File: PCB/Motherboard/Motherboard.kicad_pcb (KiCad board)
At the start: 2 copper layers, 70 x 75 mm, 14 parts, among them J1 RX input, J10 Power, J11 Conn_01x04, J2 North PWM, J3 South PWM, J4 East PWM, J5 West PWM, J6 North HALL, J7 South Hall, J8 East Hall, J9 West Hall

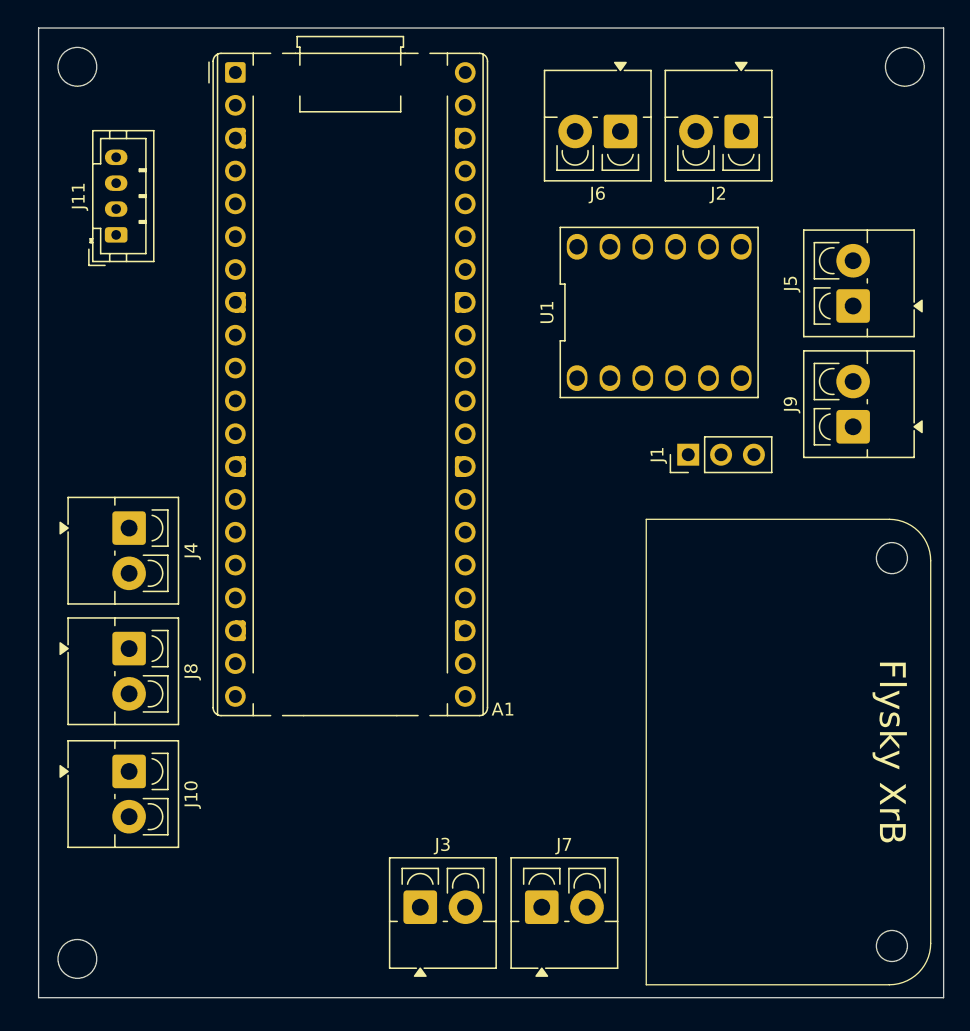
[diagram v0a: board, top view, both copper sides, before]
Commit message: daughterboard + motherboard finished
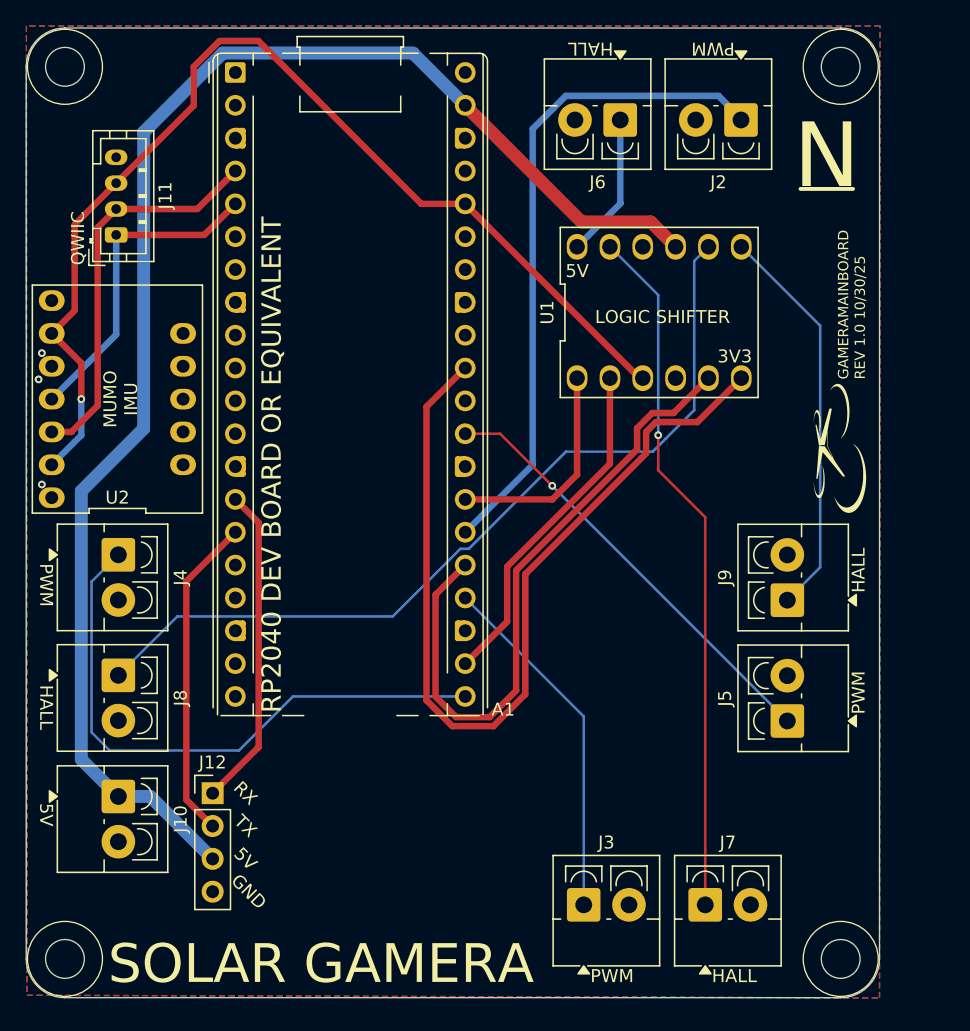
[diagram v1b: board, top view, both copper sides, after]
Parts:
- removed Flysky XrB: x6b, Custom_Footprint_Library:x6b
- removed J1: RX input, Connector_PinHeader_2.54mm:PinHeader_1x03_P2.54mm_Vertical
- added G***: LOGO, LOGO, F.Cu at (162.0, 122.5)
- added G***: LOGO, LOGO, B.Cu at (135.1, 160.1)
- added J12: Conn_01x04_Socket, Connector_PinHeader_2.54mm:PinHeader_1x04_P2.54mm_Vertical, F.Cu at (113.5, 149.2)
- added U2: ~, Custom_Footprint_Library:Mumo, F.Cu at (106.1, 118.7)
- J11: value Conn_01x04 -> QWIIC
- moved J5 32.5 mm to (157.9, 143.6)
- moved J9 14.3 mm to (157.9, 134.3)
- moved J7 12.6 mm to (151.6, 157.8)
- moved J3 12.6 mm to (142.2, 157.8)
- moved J4 2.23 mm to (106.2, 130.7)
- moved J8 2.23 mm to (106.2, 140.1)
- moved J10 2.11 mm to (110.0, 147.1)
- moved J2 0.89 mm to (154.3, 97.1)
- moved J6 0.89 mm to (145.0, 97.1)
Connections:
- A1 pad 10: SHALL3V3 -> unconnected-(A1-GPIO7-Pad10)
- A1 pad 11: EHALL3V3 -> unconnected-(A1-GPIO8-Pad11)
- A1 pad 12: WHALL3V3 -> unconnected-(A1-GPIO9-Pad12)
- A1 pad 14: PPM -> RX
- A1 pad 15: unconnected-(A1-GPIO11-Pad15) -> TX
- A1 pad 22: unconnected-(A1-GPIO17-Pad22) -> EHALL3V3
- A1 pad 25: unconnected-(A1-GPIO19-Pad25) -> SHALL3V3
- A1 pad 26: WPWM -> NPWM
- A1 pad 27: unconnected-(A1-GPIO21-Pad27) -> WHALL3V3
- A1 pad 29: NPWM -> WPWM
- A1 pad 31: unconnected-(A1-GPIO26_ADC0-Pad31) -> NHALL3V3
- A1 pad 9: NHALL3V3 -> unconnected-(A1-GPIO6-Pad9)
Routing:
- net +5V: track 0.00 -> 113.8 mm
- net +3V3: track 0.00 -> 83.6 mm, vias 0 -> 1
- net NHALL3V3: track 0.00 -> 69.7 mm
- net EHALL5V: track 0.00 -> 66.1 mm
- net SHALL5V: track 0.00 -> 54.0 mm, vias 0 -> 1
- net NPWM: track 0.00 -> 51.3 mm
- net SHALL3V3: track 0.00 -> 50.2 mm
- net EPWM: track 0.00 -> 45.8 mm
- net WPWM: track 0.00 -> 34.1 mm, vias 0 -> 1
- net WHALL5V: track 0.00 -> 30.9 mm
- net SDA: track 0.00 -> 30.6 mm
- net SPWM: track 0.00 -> 27.5 mm
- net EHALL3V3: track 0.00 -> 26.7 mm
- net TX: track 0.00 -> 25.1 mm
- net SCL: track 0.00 -> 25.0 mm
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- added copper zone on B.Cu, net GND
- added copper zone on F.Cu, net GND
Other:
- board size 70 x 75 mm -> 66 x 75 mm
- board text added: "3V3"
- board text added: "5V"
- board text added: "GAMERAMAINBOARD REV 1.0 10/30/25"
- board text added: "GND"
- board text added: "HALL"
- board text added: "LOGIC SHIFTER"
- board text added: "MUMO IMU"
- board text added: "N"
- board text added: "PWM"
- board text added: "QWIIC"
- board text added: "RP2040 DEV BOARD OR EQUIVALENT"
- board text added: "RX"
- board text added: "SOLAR GAMERA"
- board text added: "TX"
